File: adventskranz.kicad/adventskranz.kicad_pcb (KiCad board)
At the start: 2 copper layers, 70 x 70 mm, 10 parts, among them J1 Conn_01x06_Male, SW1 SW_Push

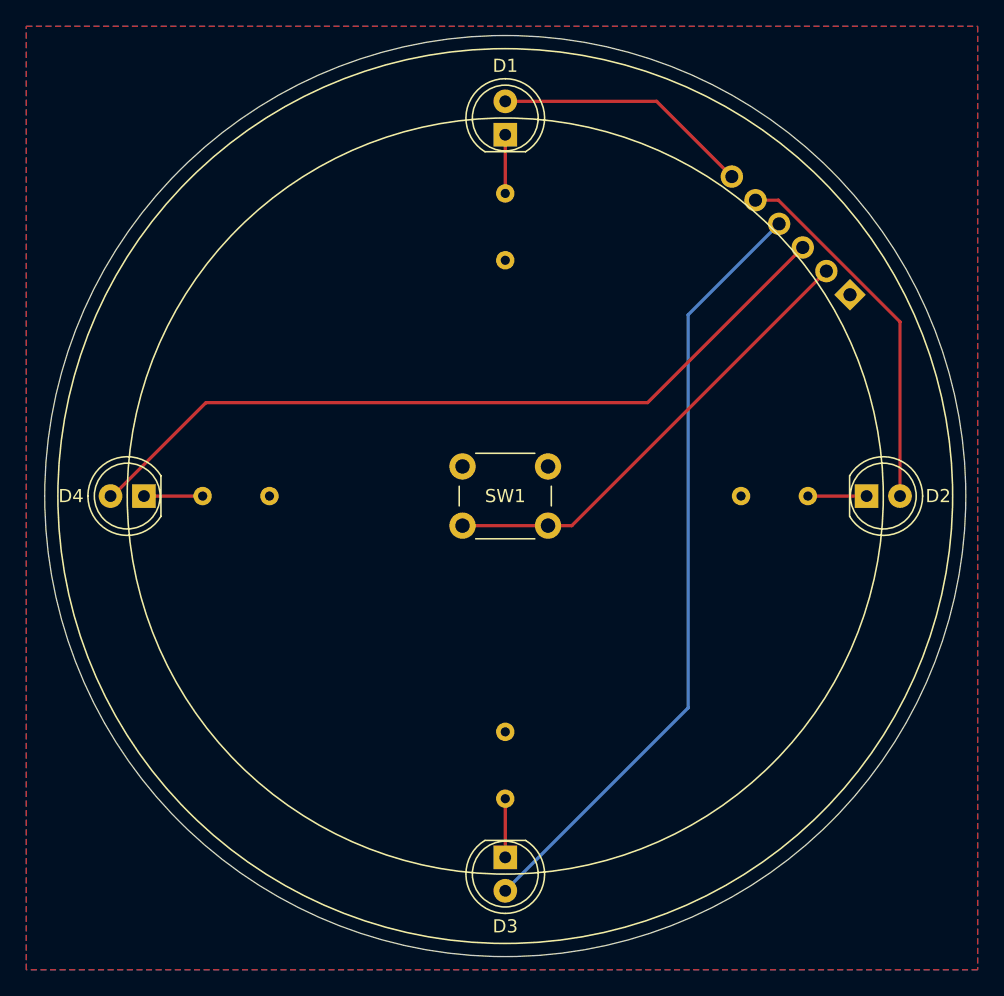
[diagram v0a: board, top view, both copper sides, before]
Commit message: Rev 2.1: add PIC for LED-control
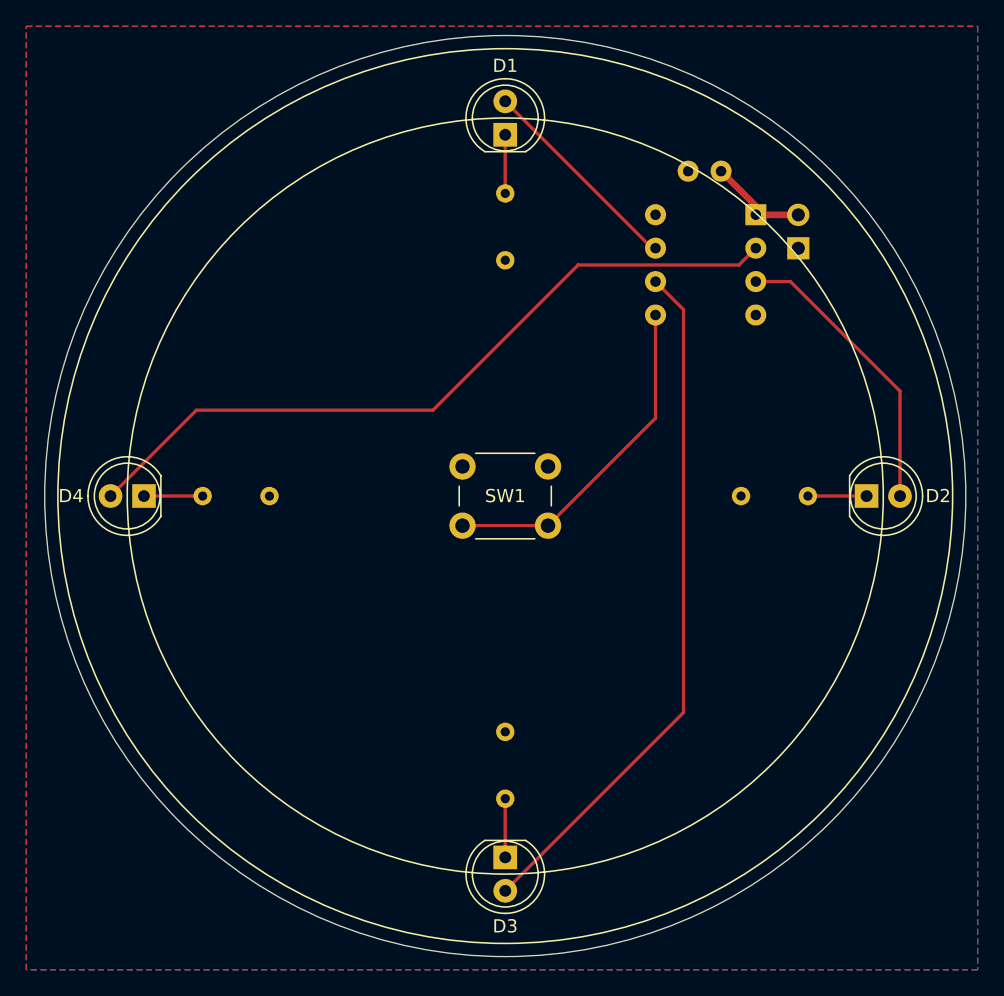
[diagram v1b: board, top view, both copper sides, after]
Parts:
- added C1: C, Capacitor_THT:C_Disc_D3.0mm_W2.0mm_P2.50mm, B.Cu at (113.9, 75.3)
- added U1: PIC12F675-IP, Package_DIP:DIP-8_W7.62mm, B.Cu at (119.0, 78.6)
- J1: value Conn_01x06_Male -> Conn_01x02_Male; footprint Connector_PinHeader_2.54mm:PinHeader_1x06_P2.54mm_Vertical -> Connector_PinHeader_2.54mm:PinHeader_1x02_P2.54mm_Vertical
- moved J1 5.28 mm to (122.3, 81.2), turned to 0 degrees
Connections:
- J1 pad 2: Net-(J1-Pad2) -> /Vdd
- SW1 pad 2: Net-(J1-Pad2) -> Net-(SW1-Pad2)
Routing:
- net Net-(J1-Pad2): track 35.7 -> 0.00 mm
- net Net-(SW1-Pad2): track 0.00 -> 25.9 mm
- net /Vdd: track 0.00 -> 6.95 mm
- net Net-(D3-Pad2): track 59.3 -> 52.8 mm
- net Net-(D2-Pad2): track 28.1 -> 22.4 mm
- net Net-(D1-Pad2): track 19.6 -> 16.0 mm
- net Net-(D4-Pad2): track 60.4 -> 57.0 mm
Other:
- board text added: "Rev 2.1"
- board text added: "Vdd"
- board text removed: "BTN"
- board text removed: "D1"
- board text removed: "D2"
- board text removed: "D3"
- board text removed: "D4"
- board text removed: "Rev 1.0"

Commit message: moved power-connector
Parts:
- moved J1 11.0 mm to (129.5, 89.5), turned to 25 degrees
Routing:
- net /Vdd: track 6.95 -> 18.0 mm
- net Net-(D2-Pad2): track 22.4 -> 21.4 mm
